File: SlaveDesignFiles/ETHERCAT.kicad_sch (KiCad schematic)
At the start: 33 parts

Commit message: 1. 在USB处，修改了type-c5V输入的定义，添加了二极管；2. 将CJA1117B-3.3替换为AMS1117-3.3；3. 分配了testpoint的封装；4. 修改了H485，can插件的PE_GNG引脚定义。
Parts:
- gave numbers to parts that had none: 33

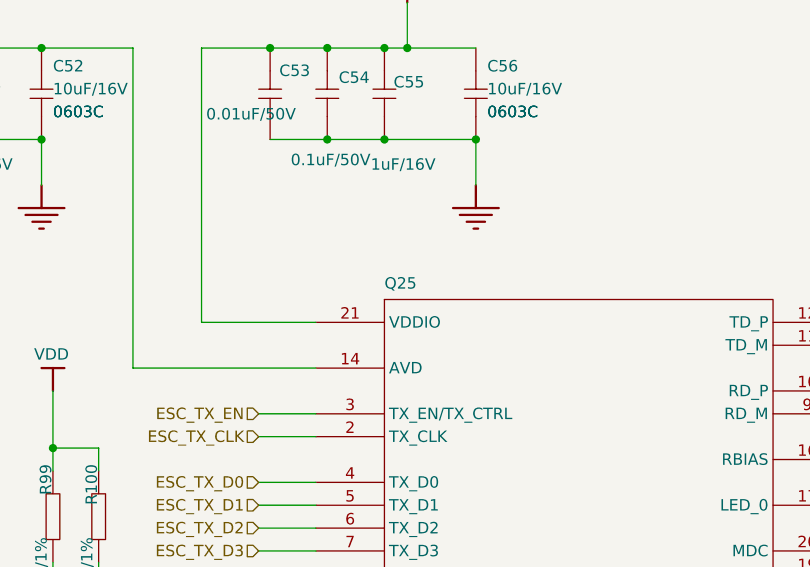
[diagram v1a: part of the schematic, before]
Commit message: Fix bugs in PWM subsheet
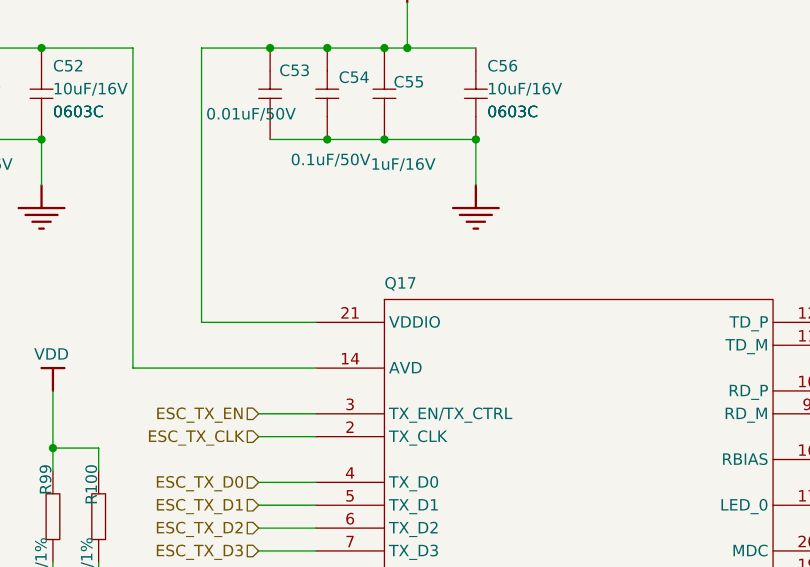
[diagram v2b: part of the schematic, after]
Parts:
- renumbered Q25 to Q17
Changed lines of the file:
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@@
 		(on_board yes)
 		(dnp no)
-		(property "Reference" "Q25"
+		(property "Reference" "Q17"
 			(at 86.36 49.53 0)
 			(effects
@@
 			(project "sheet1"
 				(path "/54840d93-b842-4275-b1cb-4ec5510cbfff/bd1d3500-042d-48a5-860b-a4b61b04c17b"
-					(reference "Q25")
+					(reference "Q17")
 					(unit 1)
 				)
